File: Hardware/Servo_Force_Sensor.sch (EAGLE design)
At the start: 1 part

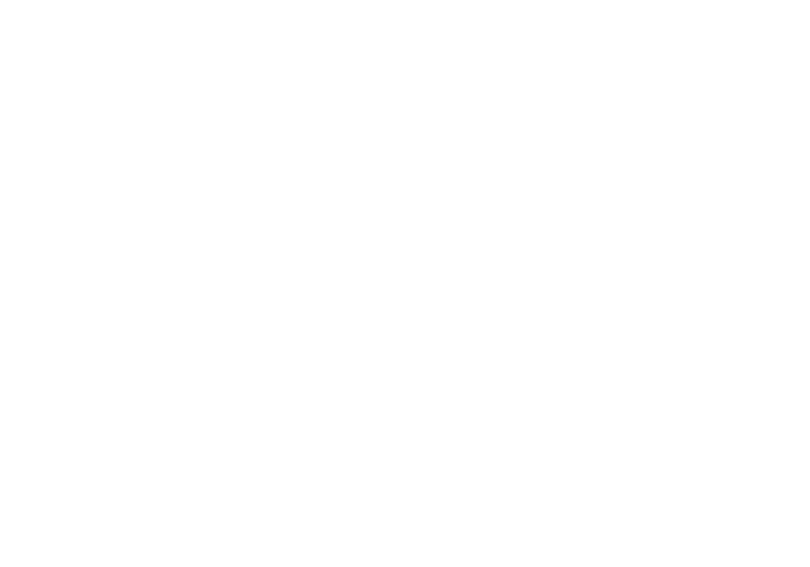
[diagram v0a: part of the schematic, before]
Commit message: library work for medium and large horns
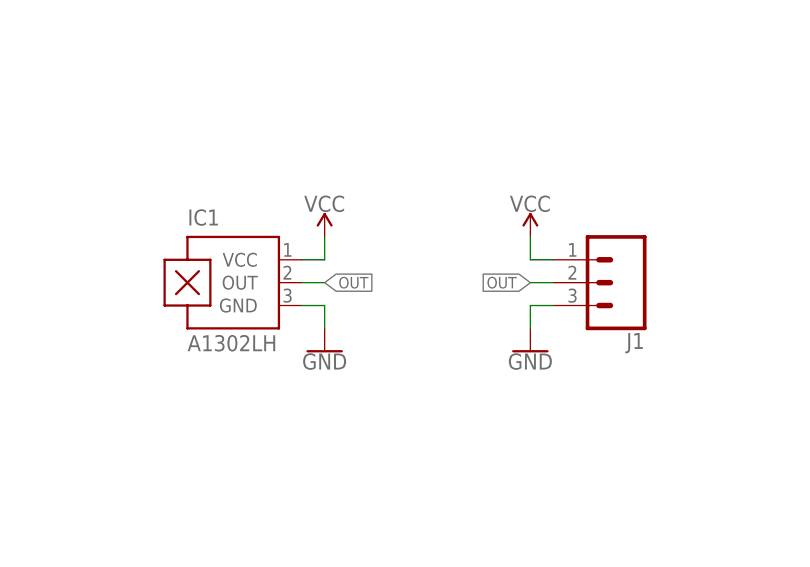
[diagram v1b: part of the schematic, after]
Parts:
- added IC1: A1302LH, allegro:A1302LH
- added J1: (no value), SparkFun-Connectors:CONN_03LONGPADS
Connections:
- new net GND: IC1.GND, J1.3
- new net OUT: IC1.OUT, J1.2
- new net VCC: IC1.VCC, J1.1
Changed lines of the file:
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@@
 <parts>
 <part name="FRAME1" library="SparkFun-Aesthetics" deviceset="FRAME-LETTER" device=""/>
+<part name="IC1" library="allegro" library_urn="urn:adsk.eagle:library:93" deviceset="A13*?" device="LH" package3d_urn="urn:adsk.eagle:package:3443/1" technology="02"/>
+<part name="GND1" library="SparkFun-PowerSymbols" deviceset="GND" device=""/>
+<part name="SUPPLY1" library="SparkFun-PowerSymbols" deviceset="VCC" device=""/>
+<part name="GND2" library="SparkFun-PowerSymbols" deviceset="GND" device=""/>
+<part name="SUPPLY2" library="SparkFun-PowerSymbols" deviceset="VCC" device=""/>
+<part name="J1" library="SparkFun-Connectors" deviceset="CONN_03" device="LONGPADS"/>
 </parts>
 <sheets>
@@
 <attribute name="DRAWING_NAME" x="162.814" y="17.78" size="2.7432" layer="94" font="vector"/>
 </instance>
+<instance part="IC1" gate="G$1" x="114.3" y="114.3" smashed="yes">
+<attribute name="NAME" x="109.22" y="120.65" size="1.778" layer="95"/>
+<attribute name="VALUE" x="109.22" y="106.68" size="1.778" layer="96"/>
+</instance>
+<instance part="GND1" gate="1" x="124.46" y="106.68" smashed="yes">
+<attribute name="VALUE" x="124.46" y="106.426" size="1.778" layer="96" align="top-center"/>
+</instance>
+<instance part="SUPPLY1" gate="G$1" x="124.46" y="119.38" smashed="yes">
+<attribute name="VALUE" x="124.46" y="122.174" size="1.778" layer="96" align="bottom-center"/>
+</instance>
+<instance part="GND2" gate="1" x="147.32" y="106.68" smashed="yes" rot="MR0">
+<attribute name="VALUE" x="147.32" y="106.426" size="1.778" layer="96" rot="MR0" align="top-center"/>
+</instance>
+<instance part="SUPPLY2" gate="G$1" x="147.32" y="119.38" smashed="yes" rot="MR0">
+<attribute name="VALUE" x="147.32" y="122.174" size="1.778" layer="96" rot="MR0" align="bottom-center"/>
+</instance>
+<instance part="J1" gate="J$1" x="157.48" y="114.3" smashed="yes" rot="R180">
+<attribute name="VALUE" x="160.02" y="121.666" size="1.778" layer="96" font="vector" rot="R180"/>
+<attribute name="NAME" x="160.02" y="108.712" size="1.778" layer="95" font="vector" rot="R180"/>
+</instance>
 </instances>
 <busses>
 </busses>
 <nets>
+<net name="VCC" class="0">
+<segment>
+<pinref part="SUPPLY1" gate="G$1" pin="VCC"/>
+<wire x1="124.46" y1="119.38" x2="124.46" y2="116.84" width="0.1524" layer="91"/>
+<pinref part="IC1" gate="G$1" pin="VCC"/>
+<wire x1="124.46" y1="116.84" x2="121.92" y2="116.84" width="0.1524" layer="91"/>
+</segment>
+<segment>
+<pinref part="SUPPLY2" gate="G$1" pin="VCC"/>
+<wire x1="147.32" y1="119.38" x2="147.32" y2="116.84" width="0.1524" layer="91"/>
+<wire x1="147.32" y1="116.84" x2="149.86" y2="116.84" width="0.1524" layer="91"/>
+<pinref part="J1" gate="J$1" pin="1"/>
+</segment>
+</net>
+<net name="GND" class="0">
+<segment>
+<pinref part="GND1" gate="1" pin="GND"/>
+<wire x1="124.46" y1="109.22" x2="124.46" y2="111.76" width="0.1524" layer="91"/>
+<pinref part="IC1" gate="G$1" pin="GND"/>
+<wire x1="124.46" y1="111.76" x2="121.92" y2="111.76" width="0.1524" layer="91"/>
+</segment>
+<segment>
+<pinref part="GND2" gate="1" pin="GND"/>
+<wire x1="147.32" y1="109.22" x2="147.32" y2="111.76" width="0.1524" layer="91"/>
+<wire x1="147.32" y1="111.76" x2="149.86" y2="111.76" width="0.1524" layer="91"/>
+<pinref part="J1" gate="J$1" pin="3"/>
+</segment>
+</net>
+<net name="OUT" class="0">
+<segment>
+<pinref part="IC1" gate="G$1" pin="OUT"/>
+<wire x1="121.92" y1="114.3" x2="124.46" y2="114.3" width="0.1524" layer="91"/>
+<label x="124.46" y="114.3" size="1.27" layer="95" xref="yes"/>
+</segment>
+<segment>
+<wire x1="149.86" y1="114.3" x2="147.32" y2="114.3" width="0.1524" layer="91"/>
+<label x="147.32" y="114.3" size="1.27" layer="95" rot="MR0" xref="yes"/>
+<pinref part="J1" gate="J$1" pin="2"/>
+</segment>
+</net>
 </nets>
 </sheet>
@@
 </schematic>
 </drawing>
+<compatibility>
+<note version="8.2" severity="warning">
+Since Version 8.2, EAGLE supports online libraries. The ids
+of those online libraries will not be understood (or retained)
+with this version.
+</note>
+<note version="8.3" severity="warning">
+Since Version 8.3, EAGLE supports URNs for individual library
+assets (packages, symbols, and devices). The URNs of those assets
+will not be understood (or retained) with this version.
+</note>
+<note version="8.3" severity="warning">
+Since Version 8.3, EAGLE supports the association of 3D packages
+with devices in libraries, schematics, and board files. Those 3D
+packages will not be understood (or retained) with this version.
+</note>
+</compatibility>
 </eagle>
